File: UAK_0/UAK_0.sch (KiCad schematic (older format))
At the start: 7 parts, among them X4 Крепежное_отверстие_М3, X5 Крепежное_отверстие_М3, X6 Крепежное_отверстие_М3, X7 Крепежное_отверстие_М3, X8 Клеммник_х2_KLS2-300-5.00-02P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

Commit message: BOOT&PRG, концевик, ЖК, звук, подсветка - без трассировки
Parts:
- added C11, C12, C13: Конденсатор_керамический, N_RLC:Конденсатор_SMD_0603, symbol elements:Конденсатор_керамический
- added HA1: Излучатель_HPA17F, N_VD_HL:Зуммер_HPA17F, symbol elements_2020:Излучатель_HPA17F
- added K1, K2: Кнопка_FSMSM, N_X:Кнопка_FSMSM, symbol elements:кнопка
- added R10, R11, R12, R13, R14, R15, R16, R5, R6, R7, R8, R9: Резистор_0,065Вт, N_RLC:Резистор_SMD_0603_0,065_Вт, symbol elements:Резистор_0,065Вт
- added RP1: Резистор_подстроечный_PVA3A103, MOTOR_IMPORT_OTK:резистор_подстроечный_PVZ3A334, symbol elements_2020:Резистор_подстроечный_PVA3A103
- added VD1: Набор_диодов_BAR43CFILM, MOTOR_VD_VT_HL:Корпус_КТ-46, symbol MOTOR_2020_components:Набор_диодов_2Д803АС9
- added VD2, VD3: Диод_шоттки_SK16, N_VD_HL:Диод_SMB, symbol elements_2020:Диод_шоттки_SK16
- added VT1, VT2, VT3: Транзистор_полевой_N-канальный_IRLML6344TR, MOTOR_VD_VT_HL:Корпус_КТ-46, symbol elements_2020:Транзистор_полевой_N-канальный_IRLML6344TR
- added X10, X9: Клеммник_х2_308-021-14, N_X:Клеммник_х2_шаг2.54, symbol elements_2020:Клеммник_х2_KLS2-300-5.00-02P-2S
- added XP1: Вилка_WF-4R, MOTOR_X:Вилка_СНП389-4ВП32-1-1, symbol MOTOR_2020_components:Вилка_СНП389-4ВП32-1-1
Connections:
- net DOOR_2: now reaches A1.1 (GND)
- net DOOR_2: now also A1.15 (GND), A1.38 (GND), A1.39 (GND), HL1.1 (GND), HL1.5 (R/W), C11.2, C12.2, C13.1, K1.1, K2.1, R12.2, R13.2, R14.2, RP1.2, RP1.3, VT1.2, VT2.2, VT3.2, X10.2, XP1.4
- net BUZZER: now reaches A1.14 (IO12)
- net BUZZER: now also R11.2
- net MC_OUT_1: now reaches A1.16 (IO13)
- net MC_OUT_1: now also R10.2
- net 3V3: now reaches A1.2 (3V3)
- net 3V3: now also R15.1, R5.1, R6.1, VD1.3
- net DOOR_SENSOR: now reaches A1.23 (IO15)
- net DOOR_SENSOR: now also C13.2, R15.2, R16.2
- net BOOT_SEL: now reaches A1.25 (IO(ноль)_BOOT)
- net BOOT_SEL: now also C12.1, R6.2, R8.2
- net LCD_DATA_7: now reaches A1.26 (IO4)
- net LCD_DATA_7: now also HL1.14 (DB7)
- net LCD_DATA_5: now reaches A1.29 (IO5)
- net LCD_DATA_5: now also HL1.12 (DB5)
- net EN_RESET: now reaches A1.3 (EN)
- net EN_RESET: now also C11.1, R5.2, R7.2
- net LCD_E: now reaches A1.30 (IO18)
- net LCD_E: now also HL1.6 (E)
- net LCD_A0: now reaches A1.31 (IO19)
- net LCD_A0: now also HL1.4 (A0)
- net LCD_DATA_4: now reaches A1.33 (IO21)
- net LCD_DATA_4: now also HL1.11 (DB4)
- net BOOT_UART_RX: now reaches A1.34 (RXD0)
- net BOOT_UART_RX: now also XP1.3
- net BOOT_UART_TX: now reaches A1.35 (TXD0)
- net BOOT_UART_TX: now also XP1.2
- net LCD_DATA_6: now reaches A1.36 (IO22)
- net LCD_DATA_6: now also HL1.13 (DB6)
- net LCD_LED: now reaches A1.37 (IO23)
- net LCD_LED: now also R9.2
- net 5V: now reaches HL1.15 (LED+)
- net 5V: now also HL1.2 (Ucc), HA1.1, VD3.2
- net at HL1.16 (LED-): now also VT1.3
- net at HL1.3 (Uo(ЖК)): now also RP1.1
- new net: K1.2, R7.1
- new net: K2.2, R8.1
- new net: VD1.1, VD1.2, XP1.1
- new net: R10.1, R13.1, VT2.1
- new net: R11.1, R14.1, VT3.1
- new net: HA1.2, VD3.1, VT3.3
- new net: R12.1, R9.1, VT1.1
- new net 12V: VD2.2, X9.1
- new net DOOR_1: R16.1, X10.1
- new net D_OUT_1: VD2.1, VT2.3, X9.2
- no-connect marks 0 -> 4
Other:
- note added: "ВВОД И РАСПРЕДЕЛЕНИЕ ПИТАНИЯ"
- note added: "ВЫБОБР BOOT И ПРОГРАММИРОВАНИЕ"
- note added: "ЖК-ДИСПЛЕЙ"
- note added: "ЗВУКОВАЯ СИГНАЛИЗАЦИЯ"
- note added: "КОНЦЕВИК ДВЕРИ"
- note added: "ПОДСВЕТКА ЛАМПЫ"
- moved on the sheet: A1, HL1, X8

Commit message: нет коммутации 220В, остальная схема есть, нет трассировка
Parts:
- added C1, C6: Конденсатор_керамический, N_RLC:Конденсатор_SMD_0603, symbol elements:Конденсатор_керамический
- added C2: Конденсатор_К53-56А-32В-22_мкФ+-10проц., MOTOR_RLC:Конденсатор_тантал_SMD_m7343, symbol MOTOR_2020_components:Конденсатор_К53-56А-32В-22_мкФ+-10проц.
- added DD1: Повторитель_M74VHC1GT125, N_DD:SC-70-5, symbol elements_2020:Повторитель_M74VHC1GT125
- added R12, R9: Резистор_0,065Вт, N_RLC:Резистор_SMD_0603_0,065_Вт, symbol elements:Резистор_0,065Вт
- added XT2, XT3, XT7: Клеммник_х2_308-021-14, N_X:Клеммник_х2_шаг2.54, symbol elements_2020:Клеммник_х2_KLS2-300-5.00-02P-2S
- added XT5: Клеммник_х2_KLS2-300-5.00-02P-2S, N_X:Клеммник_х2_шаг5, symbol elements_2020:Клеммник_х2_KLS2-300-5.00-02P-2S
- renumbered C11 to C3, C12 to C4, C13 to C5, R9 to R1, R6 to R10, R16 to R11, R7 to R13, R8 to R14, R10 to R2, R11 to R3, R12 to R4, R13 to R5, R14 to R6, R5 to R7, R15 to R8, VD2 to VD1, VD3 to VD2, VD1 to VD3, X4 to X1, X6 to X2, X5 to X3, X7 to X4, X9 to XT1, X8 to XT4, X10 to XT6
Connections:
- net DOOR_2 is gone; now on net BUTT_2: A1.1 (GND), A1.15 (GND), A1.38 (GND), A1.39 (GND), C3.2, C4.2, C5.1, HL1.1 (GND), HL1.5 (R/W), K1.1, K2.1, R4.2, R5.2, R6.2, RP1.2, RP1.3, VT1.2, VT2.2, VT3.2, XP1.4, XT6.2
- net 3V3: now also R9.1
- net 5V: now also C1.1, C2.1, DD1.5 (VCC), XT2.1
- net BUZZER: now also A1.33 (IO21); no longer A1.14 (IO12)
- net DOOR_SENSOR: now also A1.37 (IO23); no longer A1.23 (IO15)
- net LCD_A0: now also A1.23 (IO15); no longer A1.31 (IO19)
- net LCD_DATA_4: now also A1.26 (IO4); no longer A1.33 (IO21)
- net LCD_DATA_6: now also A1.30 (IO18); no longer A1.36 (IO22)
- net LCD_DATA_7: now also A1.31 (IO19); no longer A1.26 (IO4)
- net LCD_E: now also A1.24 (IO2); no longer A1.30 (IO18)
- net LCD_LED: now also A1.16 (IO13); no longer A1.37 (IO23)
- net MC_OUT_1: now also A1.11 (IO26); no longer A1.16 (IO13)
- net EXT_BUTTON: now reaches A1.12 (IO27)
- net EXT_BUTTON: now also C6.2, R12.2, R9.2
- net BUTT_2: now reaches HL1.10 (DB3)
- net BUTT_2: now also HL1.7 (DB0), HL1.8 (DB1), HL1.9 (DB2), C1.2, C2.2, C6.1, DD1.1 (~OE), DD1.3 (GND), XT3.1, XT3.2, XT7.2
- new net 0V_RES: XT5.2
- new net 12V_RES: XT5.1
- new net BUTT_1: R12.1, XT7.1
- new net LED_OUT: DD1.4 (OUT), XT2.2
- new net LED_WS2812: A1.36 (IO22), DD1.2 (IN)
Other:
- note added: "ВНЕШНЯЯ КНОПКА"
- note added: "НА СВЕТОДИОДНУЮ ЛЕНТУ WS2812"
- note added: "ПОДСВЕТКА ЛАМПЫ (ОТКРЫТЫЙ СТОК)"
- note added: "СДВОЕННЫЙ"
- note removed: "ПОДСВЕТКА ЛАМПЫ"
- moved on the sheet: C5, HL1, R1, R11, R4, R8, RP1, VT1, XT6

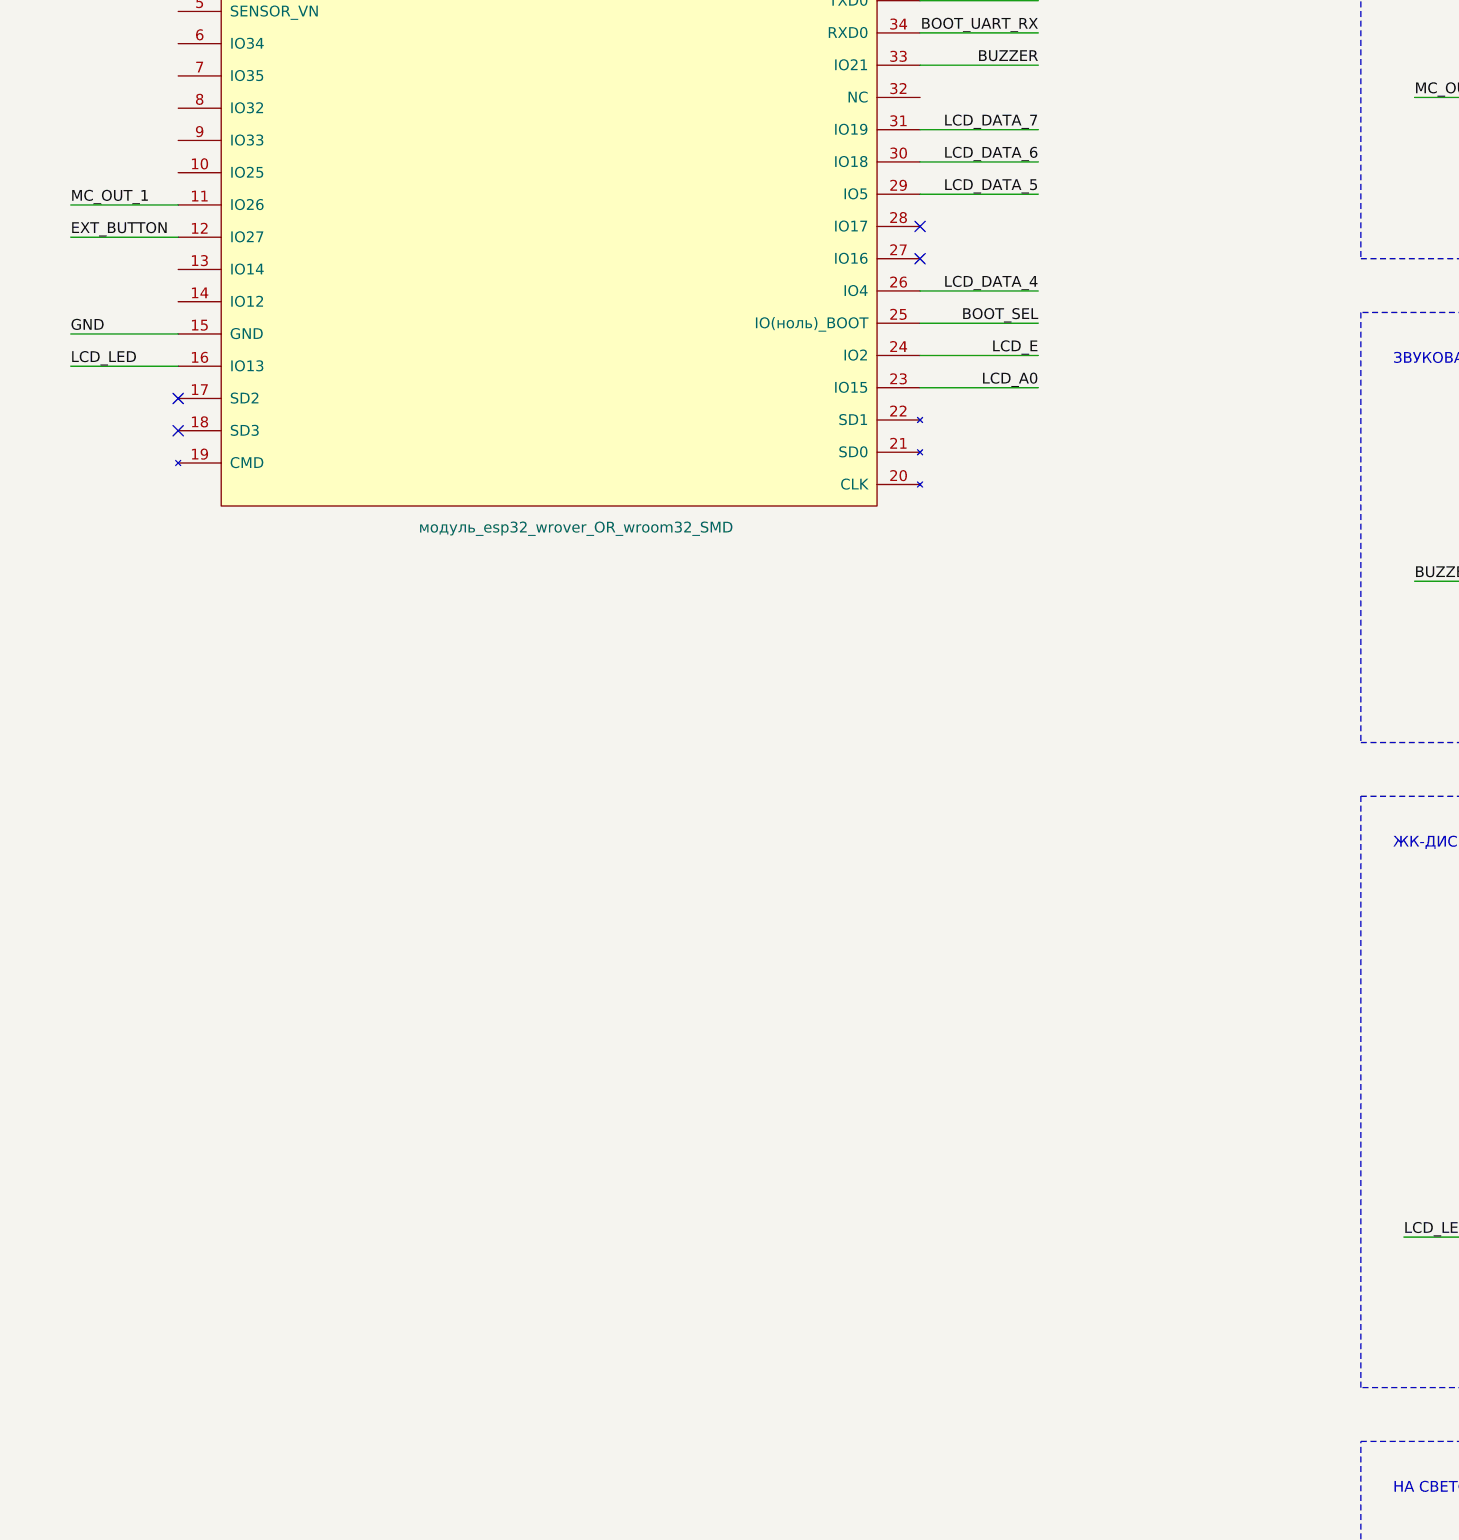
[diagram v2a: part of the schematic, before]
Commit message: подготовлена схема, нет трассировки
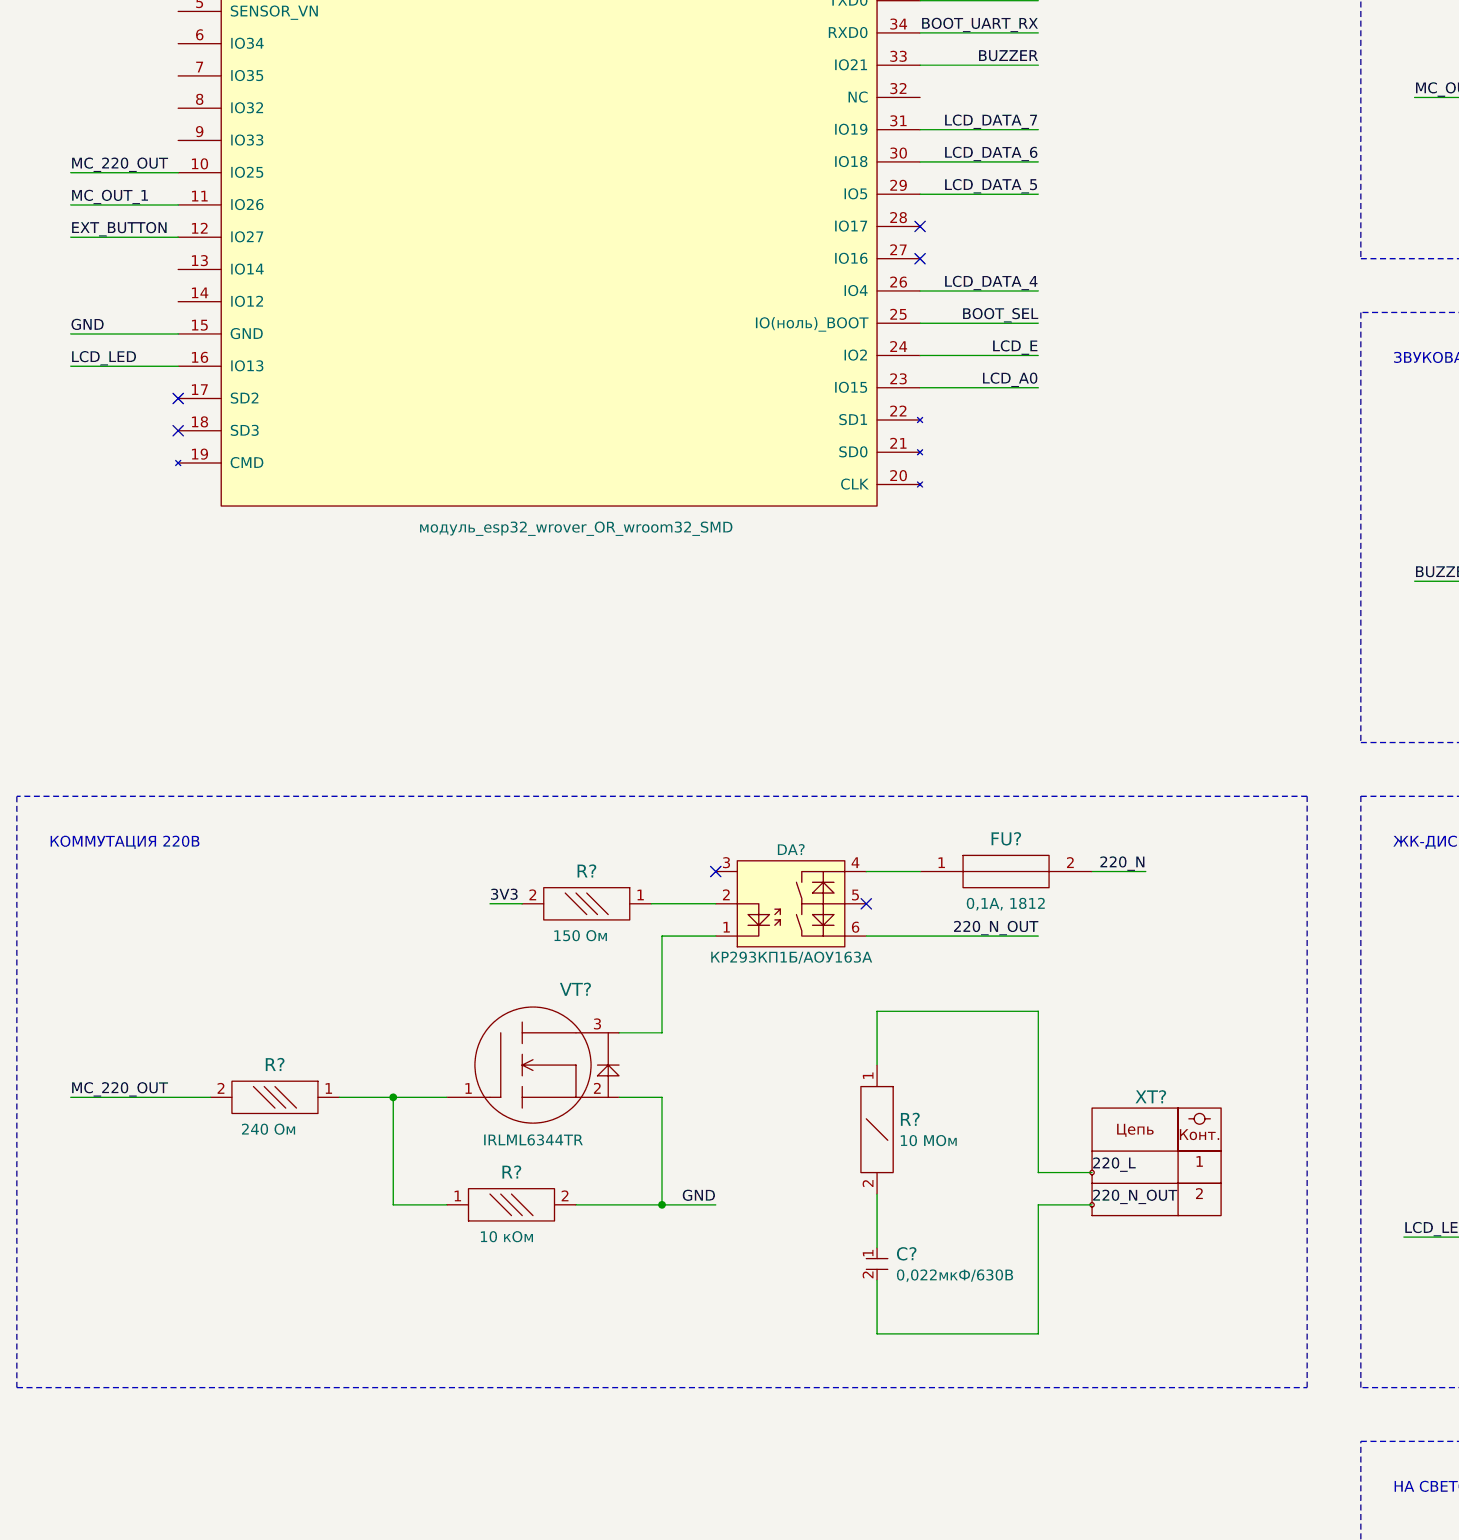
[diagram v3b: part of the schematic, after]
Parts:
- added C?: Конденсатор_керамический, N_RLC:Конденсатор_SMD_1210, symbol elements:Конденсатор_керамический
- added DA?: МОП-реле_КР293КП1Б, symbol elements_2020:МОП-реле_КР293КП1Б
- added FU?: Предохранитель, N_RLC:Предохранитель_SMD_1812, symbol elements:Предохранитель
- added R? (x3): Резистор_0,065Вт, N_RLC:Резистор_SMD_0603_0,065_Вт, symbol elements:Резистор_0,065Вт
- added R?: Резистор_0,25Вт, N_RLC:Резистор_SMD_1206-0,25_Вт, symbol elements:Резистор_0,25Вт
- added VT?: Транзистор_полевой_N-канальный_IRLML6344TR, MOTOR_VD_VT_HL:Корпус_КТ-46, symbol elements_2020:Транзистор_полевой_N-канальный_IRLML6344TR
- added XT?: Клеммник_х2_KLS2-300-5.00-02P-2S, N_X:Клеммник_х2_шаг5, symbol elements_2020:Клеммник_х2_KLS2-300-5.00-02P-2S
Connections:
- net 220_L: now also R?.1, XT?.1
- net 220_N: now also FU?.2
- net 3V3: now also R?.2
- net BUTT_2: now also R?.2, VT?.2
- net MC_220_OUT: now reaches A1.10 (IO25)
- net MC_220_OUT: now also R?.2
- new net: DA?.4, FU?.1
- new net: DA?.1, VT?.3
- new net: DA?.2, R?.1
- new net: R?.1, R?.1, VT?.1
- new net: C?.1, R?.2
- new net 220_N_OUT: C?.2, DA?.6, XT?.2
- no-connect marks 4 -> 6
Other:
- note added: "КОММУТАЦИЯ 220В"
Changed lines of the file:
@@
 Text Notes 10800 9850 0    50   ~ 0
 СДВОЕННЫЙ
+$Comp
+L elements:Предохранитель FU?
+U 1 1 5F560616
+P 5350 5600
+AR Path="/5F560616" Ref="FU?"  Part="1"
+AR Path="/5F540B17/5F560616" Ref="FU?"  Part="1"
+F 0 "FU?" H 5350 5750 60  0000 C CNN
+F 1 "Предохранитель" H 5350 5450 60  0001 C CNN
+F 2 "N_RLC:Предохранитель_SMD_1812" H 5350 5600 60  0001 C CNN
+F 3 "" H 5350 5600 60  0001 C CNN
+F 4 "0,1А, 1812" H 5350 5450 50  0000 C CNN "INFO"
+F 5 "https://www.chipdip.ru/product/mf-msmf010" H 5350 5600 50  0001 C CNN "LINK"
+	1    5350 5600
+	1    0    0    -1
+$EndComp
+$Comp
+L elements_2020:Клеммник_х2_KLS2-300-5.00-02P-2S XT?
+U 1 1 5F5696D9
+P 5750 7000
+F 0 "XT?" H 5400 7350 60  0000 L CNN
+F 1 "Клеммник_х2_KLS2-300-5.00-02P-2S" H 5440 6740 60  0001 C CNN
+F 2 "N_X:Клеммник_х2_шаг5" H 5175 7275 60  0001 C CNN
+F 3 "" H 5175 7275 60  0001 C CNN
+	1    5750 7000
+	-1   0    0    -1
+$EndComp
+Text Label 5750 7000 0    50   ~ 0
+220_L
+$Comp
+L elements_2020:МОП-реле_КР293КП1Б DA?
+U 1 1 5F56E7B1
+P 4100 5900
+F 0 "DA?" H 4350 5500 50  0000 C CNN
+F 1 "МОП-реле_КР293КП1Б" H 4000 6150 50  0001 C CNN
+F 2 "" H 4100 5900 50  0001 C CNN
+F 3 "" H 4100 5900 50  0001 C CNN
+F 4 "КР293КП1Б/АОУ163А" H 4350 6000 50  0000 C CNN "INFO"
+F 5 "https://www.chipdip.ru/product/kr293kp1b" H 4350 6100 50  0001 C CNN "LINK"
+	1    4100 5900
+	1    0    0    1
+$EndComp
+Text Label 6000 5600 2    50   ~ 0
+220_N
+Wire Wire Line
+	6000 5600 5750 5600
+NoConn ~ 4700 5750
+NoConn ~ 4000 5600
+Wire Wire Line
+	4700 5900 5500 5900
+Text Label 5500 5900 2    50   ~ 0
+220_N_OUT
+Text Label 5750 7150 0    50   ~ 0
+220_N_OUT
+$Comp
+L elements:Резистор_0,065Вт R?
+U 1 1 5F5B8E8E
+P 3400 5750
+AR Path="/5F540B17/5F5B8E8E" Ref="R?"  Part="1"
+AR Path="/5F5B8E8E" Ref="R?"  Part="1"
+F 0 "R?" H 3350 5900 60  0000 L CNN
+F 1 "Резистор_0,065Вт" H 3400 5600 60  0001 C CNN
+F 2 "N_RLC:Резистор_SMD_0603_0,065_Вт" H 3400 5750 60  0001 C CNN
+F 3 "" H 3400 5750 60  0001 C CNN
+F 4 "150 Ом" H 3300 5600 50  0000 L CNN "INFO"
+F 5 "" H 3400 5898 50  0001 C CNN "LINK"
+	1    3400 5750
+	-1   0    0    -1
+$EndComp
+Wire Wire Line
+	3700 5750 4000 5750
+Wire Wire Line
+	3100 5750 2950 5750
+Text Label 4000 7150 2    50   ~ 0
+GND
+Connection ~ 3750 7150
+Wire Wire Line
+	3750 7150 4000 7150
+Text Label 1000 6650 0    50   ~ 0
+MC_220_OUT
+Wire Wire Line
+	1000 6650 1650 6650
+Wire Wire Line
+	3750 7150 3350 7150
+Wire Wire Line
+	3750 6650 3750 7150
+Wire Wire Line
+	3550 6650 3750 6650
+Wire Wire Line
+	2500 6650 2750 6650
+Connection ~ 2500 6650
+Wire Wire Line
+	2500 6650 2500 7150
+Wire Wire Line
+	2500 7150 2750 7150
+Wire Wire Line
+	2250 6650 2500 6650
+$Comp
+L elements:Резистор_0,065Вт R?
+U 1 1 5F5D0ED9
+P 3050 7150
+AR Path="/5F540B17/5F5D0ED9" Ref="R?"  Part="1"
+AR Path="/5F5D0ED9" Ref="R?"  Part="1"
+F 0 "R?" H 3000 7000 60  0000 L CNN
+F 1 "Резистор_0,065Вт" H 3050 7000 60  0001 C CNN
+F 2 "N_RLC:Резистор_SMD_0603_0,065_Вт" H 3050 7150 60  0001 C CNN
+F 3 "" H 3050 7150 60  0001 C CNN
+F 4 "10 кОм" H 2900 7300 50  0000 L CNN "INFO"
+F 5 "" H 3050 7298 50  0001 C CNN "LINK"
+	1    3050 7150
+	1    0    0    1
+$EndComp
+$Comp
+L elements:Резистор_0,065Вт R?
+U 1 1 5F5D0EE5
+P 1950 6650
+AR Path="/5F540B17/5F5D0EE5" Ref="R?"  Part="1"
+AR Path="/5F5D0EE5" Ref="R?"  Part="1"
+F 0 "R?" H 1900 6800 60  0000 L CNN
+F 1 "Резистор_0,065Вт" H 1950 6500 60  0001 C CNN
+F 2 "N_RLC:Резистор_SMD_0603_0,065_Вт" H 1950 6650 60  0001 C CNN
+F 3 "" H 1950 6650 60  0001 C CNN
+F 4 "240 Ом" H 1850 6500 50  0000 L CNN "INFO"
+F 5 "" H 1950 6798 50  0001 C CNN "LINK"
+	1    1950 6650
+	-1   0    0    -1
+$EndComp
+$Comp
+L elements_2020:Транзистор_полевой_N-канальный_IRLML6344TR VT?
+U 1 1 5F5D0EF1
+P 3000 6650
+F 0 "VT?" H 3350 7150 60  0000 C CNN
+F 1 "Транзистор_полевой_N-канальный_IRLML6344TR" H 3200 6400 60  0001 C CNN
+F 2 "MOTOR_VD_VT_HL:Корпус_КТ-46" H 3075 7325 60  0001 C CNN
+F 3 "" H 3000 6650 60  0001 C CNN
+F 4 "https://www.chipdip.ru/product/irlml6344trpbf" H 3025 7500 50  0001 C CNN "LINK"
+F 5 "IRLML6344TR" H 3150 6450 50  0000 C CNN "INFO"
+	1    3000 6650
+	1    0    0    -1
+$EndComp
+Wire Wire Line
+	3550 6350 3750 6350
+Wire Wire Line
+	4000 5900 3750 5900
+Wire Wire Line
+	3750 5900 3750 6350
+Wire Wire Line
+	4700 5600 4950 5600
+Text Label 1000 2350 0    50   ~ 0
+MC_220_OUT
+Wire Wire Line
+	1000 2350 1500 2350
+$Comp
+L elements:Резистор_0,25Вт R?
+U 1 1 5F6B16D8
+P 4750 6800
+F 0 "R?" V 4705 6903 60  0000 L CNN
+F 1 "Резистор_0,25Вт" H 4750 6650 60  0001 C CNN
+F 2 "N_RLC:Резистор_SMD_1206-0,25_Вт" H 4750 6800 60  0001 C CNN
+F 3 "" H 4750 6800 60  0001 C CNN
+F 4 "10 МОм" V 4803 6903 50  0000 L CNN "INFO"
+F 5 "https://www.chipdip.ru/product0/9000079814" H 4750 6800 50  0001 C CNN "LINK"
+	1    4750 6800
+	0    1    1    0
+$EndComp
+Wire Wire Line
+	5500 7000 5750 7000
+Wire Wire Line
+	5500 7150 5750 7150
+Wire Notes Line
+	6750 8000 6750 5250
+Wire Notes Line
+	6750 5250 750  5250
+Wire Notes Line
+	750  5250 750  8000
+Wire Notes Line
+	750  8000 6750 8000
+Text Notes 900  5500 0    50   ~ 0
+КОММУТАЦИЯ 220В
+$Comp
+L elements:Конденсатор_керамический C?
+U 1 1 5F6EF61F
+P 4750 7400
+AR Path="/5F6EF61F" Ref="C?"  Part="1"
+AR Path="/5F540B17/5F6EF61F" Ref="C?"  Part="1"
+F 0 "C?" V 4730 7488 60  0000 L CNN
+F 1 "Конденсатор_керамический" H 4850 7300 60  0001 C CNN
+F 2 "N_RLC:Конденсатор_SMD_1210" H 4750 7400 60  0001 C CNN
+F 3 "" H 4750 7400 60  0001 C CNN
+F 4 "0,022мкФ/630В" V 4828 7488 50  0000 L CNN "INFO"
+F 5 "https://www.chipdip.ru/product/grm32qr72j223k" H 4750 7400 50  0001 C CNN "LINK"
+	1    4750 7400
+	0    1    1    0
+$EndComp
+Wire Wire Line
+	4750 7100 4750 7350
+Wire Wire Line
+	4750 7500 4750 7750
+Wire Wire Line
+	4750 7750 5500 7750
+Wire Wire Line
+	5500 7150 5500 7750
+Wire Wire Line
+	4750 6500 4750 6250
+Wire Wire Line
+	4750 6250 5500 6250
+Wire Wire Line
+	5500 6250 5500 7000
+Text Label 2950 5750 0    50   ~ 0
+3V3
 $EndSCHEMATC
